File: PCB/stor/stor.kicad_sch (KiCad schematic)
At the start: 1 part, among them U1 STM32H723VGT6

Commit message: all sketched except power section
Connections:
- net GND: now reaches U1.10 (VSS)
- net GND: now also U1.19 (VSSA)
- net PH0: now reaches U1.12 (PH0-OSC_IN)
- net PH1: now reaches U1.13 (PH1-OSC_OUT)
- net VREF: now reaches U1.20 (VREF+)
- net VCAP1: now reaches U1.48 (VCAP)
- net SWDIO: now reaches U1.72 (PA13)
- net VCAP2: now reaches U1.73 (VCAP)
- net SWCLK: now reaches U1.76 (PA14)
- net PC14: now reaches U1.8 (PC14-OSC32_IN)
- net PC15: now reaches U1.9 (PC15-OSC32_OUT)
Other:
- note added: "2.2uf to gnd each"
- note added: "??"
- note added: "Crystal"
- note added: "swd debugging breakout"

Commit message: gnda, vss
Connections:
- net GND: now also U1.26 (VSS), U1.49 (VSS), U1.74 (VSS), U1.99 (VSS); no longer U1.19 (VSSA)
- new net GNDA: U1.19 (VSSA)

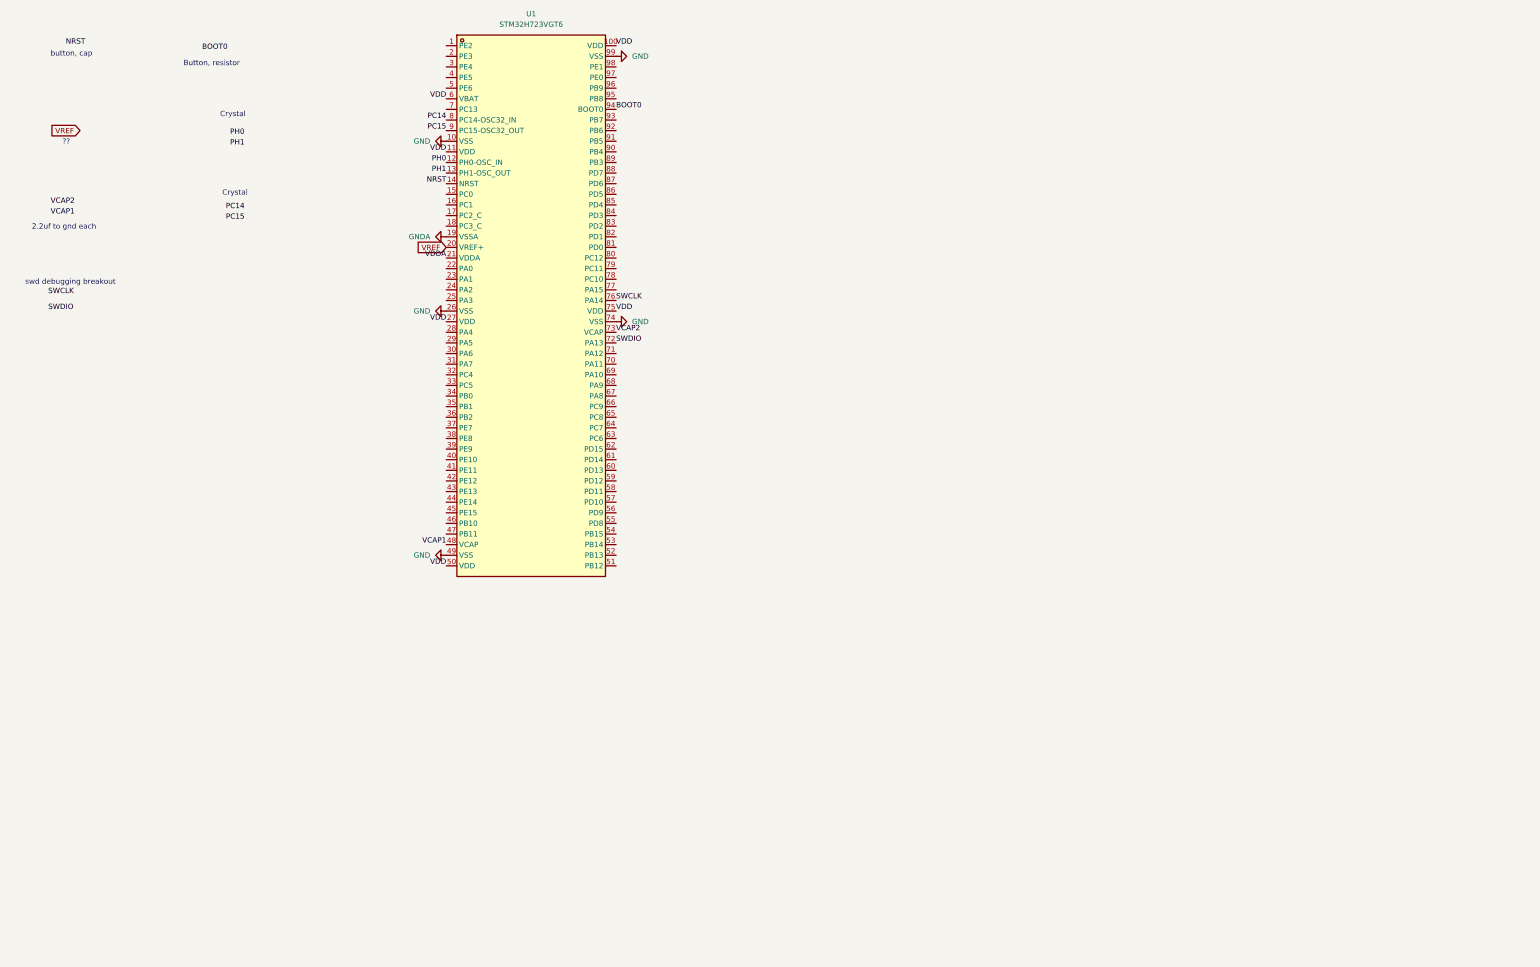
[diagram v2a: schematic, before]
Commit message: buck sourced
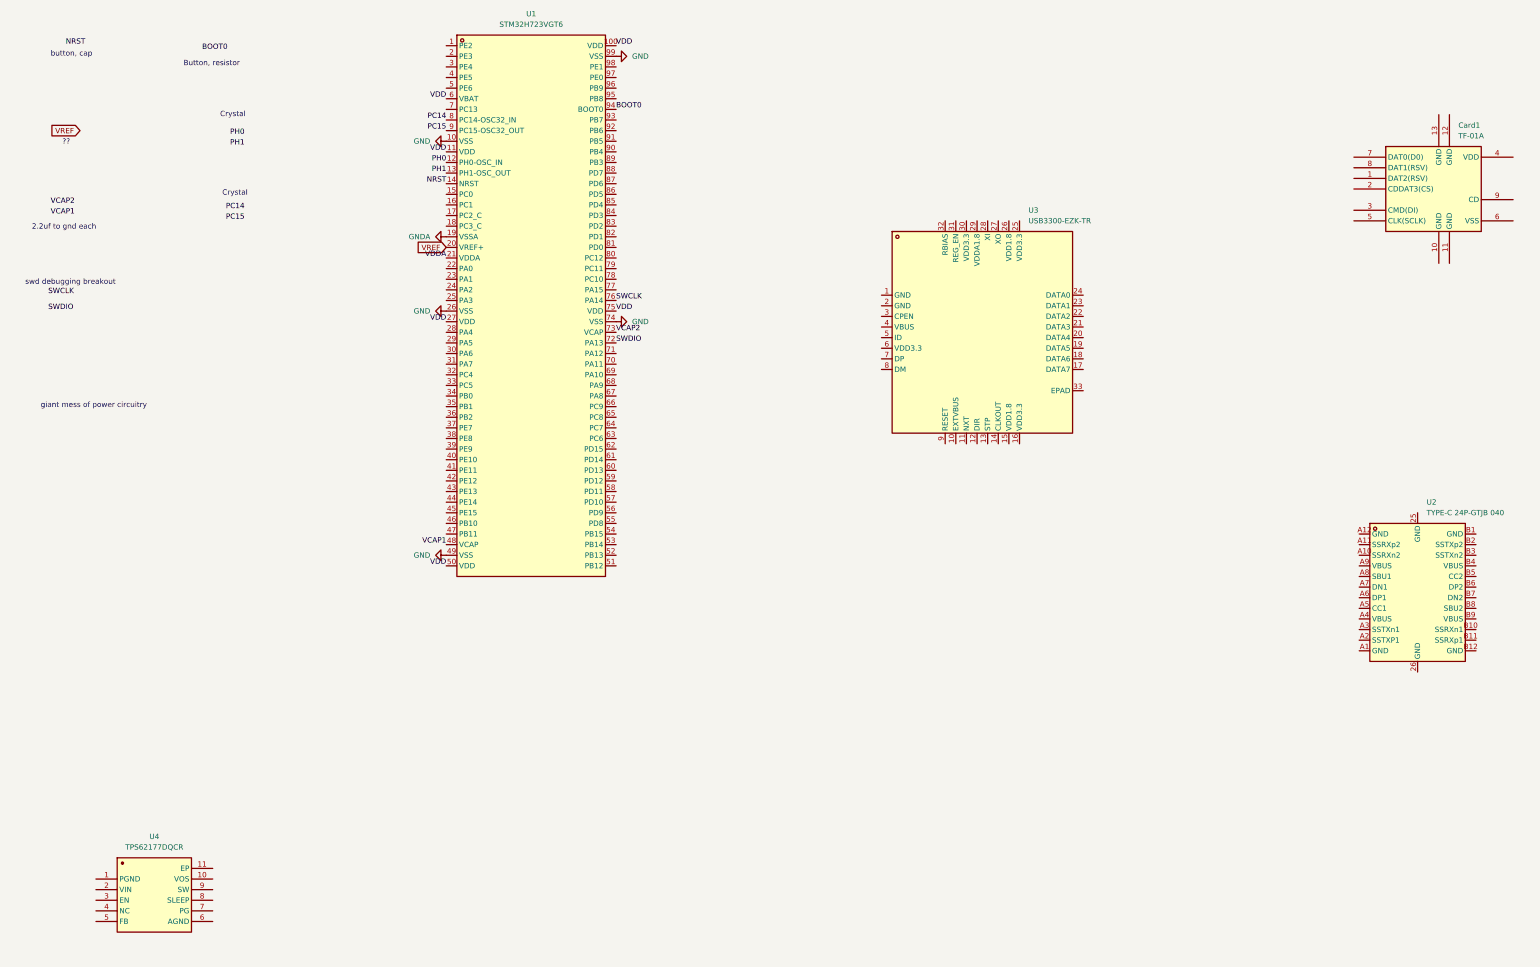
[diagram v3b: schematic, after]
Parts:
- added Card1: TF-01A, easyeda2kicad:TF-SMD_TF-01A, symbol easyeda2kicad:TF-01A
- added U2: TYPE-C 24P-GTJB 040, easyeda2kicad:USB-C-SMD_TYPE-C-24P-GTJB-040, symbol easyeda2kicad:TYPE-C24P-GTJB040
- added U3: USB3300-EZK-TR, easyeda2kicad:QFN-32_L5.0-W5.0-P0.50-BL-EP3.4, symbol easyeda2kicad:USB3300-EZK-TR
- added U4: TPS62177DQCR, easyeda2kicad:WSON-10_L3.0-W2.0-P0.50-BL-EP, symbol easyeda2kicad:TPS62177DQCR
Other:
- note added: "giant mess of power circuitry"

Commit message: smal
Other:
- note added: "8 100nF caps"
- note added: "Power"
- note removed: "giant mess of power circuitry"
- moved on the sheet: U2, U4
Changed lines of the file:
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@@
 	(generator_version "10.0")
 	(paper "A3")
-	(text "giant mess of power circuitry"
-		(exclude_from_sim no)
-		(at 32.512 108.966 0)
+	(rectangle
+		(start 30.48 180.34)
+		(end 153.67 241.3)
+		(stroke
+			(width 0)
+			(type default)
+		)
+		(fill
+			(type none)
+		)
+	)
+	(text "8 100nF caps"
+		(exclude_from_sim no)
+		(at 58.928 203.2 0)
 		(effects
 			(font
@@
 			(font
 				(size 1.27 1.27)
+			)
+		)
+	)
+	(text "Power"
+		(exclude_from_sim no)
+		(at 39.878 184.404 0)
+		(effects
+			(font
+				(size 2.54 2.54)
 			)
 		)
@@
 	(symbol
 		(lib_id "easyeda2kicad:TPS62177DQCR")
-		(at 46.99 226.06 0)
+		(at 118.11 212.09 0)
 		(unit 1)
 		(body_style 1)
@@
 		(fields_autoplaced yes)
 		(property "Reference" "U4"
-			(at 46.99 212.09 0)
+			(at 118.11 198.12 0)
 			(show_name no)
 			(do_not_autoplace no)
@@
 		)
 		(property "Value" "TPS62177DQCR"
-			(at 46.99 214.63 0)
+			(at 118.11 200.66 0)
 			(show_name no)
 			(do_not_autoplace no)
@@
 		)
 		(property "Footprint" "easyeda2kicad:WSON-10_L3.0-W2.0-P0.50-BL-EP"
-			(at 46.99 240.03 0)
+			(at 118.11 226.06 0)
 			(hide yes)
 			(show_name no)
@@
 		)
 		(property "Datasheet" "https://lcsc.com/product-detail/DC-DC-Converters_TI_TPS62177DQCR_TPS62177DQCR_C91241.html"
-			(at 46.99 242.57 0)
+			(at 118.11 228.6 0)
 			(hide yes)
 			(show_name no)
@@
 		)
 		(property "Description" ""
-			(at 46.99 226.06 0)
+			(at 118.11 212.09 0)
 			(hide yes)
 			(show_name no)
@@
 		)
 		(property "Manufacturer" "TI(德州仪器)"
-			(at 46.99 245.11 0)
+			(at 118.11 231.14 0)
 			(hide yes)
 			(show_name no)
@@
 		)
 		(property "MPN" "TPS62177DQCR"
-			(at 46.99 247.65 0)
+			(at 118.11 233.68 0)
 			(hide yes)
 			(show_name no)
@@
 		)
 		(property "LCSC Part" "C91241"
-			(at 46.99 250.19 0)
+			(at 118.11 236.22 0)
 			(hide yes)
 			(show_name no)
@@
 	(symbol
 		(lib_id "easyeda2kicad:TYPE-C24P-GTJB040")
-		(at 349.25 153.67 0)
+		(at 260.35 165.1 0)
 		(unit 1)
 		(body_style 1)
@@
 		(fields_autoplaced yes)
 		(property "Reference" "U2"
-			(at 351.3933 132.08 0)
+			(at 262.4933 143.51 0)
 			(show_name no)
 			(do_not_autoplace no)
@@
 		)
 		(property "Value" "TYPE-C 24P-GTJB 040"
-			(at 351.3933 134.62 0)
+			(at 262.4933 146.05 0)
 			(show_name no)
 			(do_not_autoplace no)
@@
 		)
 		(property "Footprint" "easyeda2kicad:USB-C-SMD_TYPE-C-24P-GTJB-040"
-			(at 349.25 180.34 0)
+			(at 260.35 191.77 0)
 			(hide yes)
 			(show_name no)
@@
 		)
 		(property "Datasheet" "https://www.lcsc.com/datasheet/C3151751.pdf"
-			(at 349.25 182.88 0)
+			(at 260.35 194.31 0)
 			(hide yes)
 			(show_name no)
@@
 		)
 		(property "Description" ""
-			(at 349.25 153.67 0)
+			(at 260.35 165.1 0)
 			(hide yes)
 			(show_name no)
@@
 		)
 		(property "Manufacturer" "SHOU HAN(首韩)"
-			(at 349.25 185.42 0)
+			(at 260.35 196.85 0)
 			(hide yes)
 			(show_name no)
@@
 		)
 		(property "MPN" "TYPE-C 24P-GTJB 040"
-			(at 349.25 187.96 0)
+			(at 260.35 199.39 0)
 			(hide yes)
 			(show_name no)
@@
 		)
 		(property "LCSC Part" "C3151751"
-			(at 349.25 190.5 0)
-			(hide yes)
-			(show_name no)
+			(at 260.35 201.93 0)
+			(hide yes)
+			(show_name no)

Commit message: stm and friends complete
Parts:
- added C1, C2: 2.2uF, easyeda2kicad:C0402, symbol easyeda2kicad:CL05A225KO5NQNC
- added C10, C15, C3, C4, C5, C6, C7, C8, C9: 100nF, easyeda2kicad:C0402, symbol easyeda2kicad:CC0402KRX7R7BB104
- added C11, C12: 10pF, easyeda2kicad:C0402, symbol easyeda2kicad:CC0402JRNPO9BN100
- added C13, C14: 12pF, easyeda2kicad:C0402, symbol easyeda2kicad:CC0402JRNPO9BN120
- added J1: Conn_01x04_Socket, symbol Connector:Conn_01x04_Socket
- added R1: 10k, easyeda2kicad:R0402, symbol easyeda2kicad:RC0402FR-0710KL
- added SW1, SW2: TS1603-TZ38HBM, easyeda2kicad:SW-SMD_4P-L4.5-W4.5-P3.00-LS6.8, symbol easyeda2kicad:TS1603-TZ38HBM
- added X1: 25mhz, easyeda2kicad:CRYSTAL-SMD_4P-L3.2-W2.5-BL, symbol easyeda2kicad:X322525MOB4SI
- added X2: 32.768k, easyeda2kicad:OSC-SMD_L3.2-W1.5, symbol easyeda2kicad:SC-32S32.768kHz20PPM12.5pF
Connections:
- net GNDA is gone; now on net GND: U1.19 (VSSA)
- net VDDA is gone; now on net VDD: U1.21 (VDDA)
- net BOOT0: now also R1.2, SW2.1 (A), SW2.2 (B)
- net GND: now also C1.1, C10.1, C11.1, C12.1, C13.1, C14.1, C15.1, C2.1, C3.1, C4.1, C5.1, C6.1, C7.1, C8.1, C9.1, J1.1 (Pin_1), R1.1, SW1.3 (C), SW1.4 (D), X1.2 (GND), X1.4 (GND)
- net NRST: now also C15.2, SW1.1 (A), SW1.2 (B)
- net PC14: now also C13.2, X2.2
- net PC15: now also C14.2, X2.1
- net PH0: now also C12.2, X1.3 (OSC2)
- net PH1: now also C11.2, X1.1 (OSC1)
- net SWCLK: now also J1.2 (Pin_2)
- net SWDIO: now also J1.3 (Pin_3)
- net VCAP1: now also C2.2
- net VCAP2: now also C1.2
- net VDD: now also C10.2, C3.2, C4.2, C5.2, C6.2, C7.2, C8.2, C9.2, J1.4 (Pin_4), SW2.3 (C), SW2.4 (D)
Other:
- note added: "STM and friends"
- note removed: "2.2uf to gnd each"
- note removed: "8 100nF caps"
- note removed: "Button, resistor"
- note removed: "Crystal"
- note removed: "swd debugging breakout"
- moved on the sheet: U4

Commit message: pmic done
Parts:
- added C16: 2.2uF, easyeda2kicad:C0402, symbol easyeda2kicad:CL05A225KO5NQNC
- added C17: 22uF, easyeda2kicad:C0402, symbol easyeda2kicad:GRM158C80G226ME01D
- added L1: 10uH, easyeda2kicad:IND-SMD_L3.2-W2.5_CKST322512-2.2UH, symbol easyeda2kicad:XRTC322512S100MBCA
- added R2, R3: 5.1k, easyeda2kicad:R0402, symbol easyeda2kicad:RC0402FR-075K1L
- added R4: 100k, easyeda2kicad:R0402, symbol easyeda2kicad:RC0402FR-07100KL
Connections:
- net GND: now also U2.25 (GND), U2.A1 (GND), U2.A12 (GND), U2.B1 (GND), U2.B12 (GND), U4.1 (PGND), U4.11 (EP), U4.4 (NC), U4.5 (FB), U4.6 (AGND), C16.2, C17.1, R2.1, R3.1
- net VDD: now also U4.10 (VOS), C17.2, L1.2, R4.2
- net VBUS: now reaches U4.2 (VIN)
- net VBUS: now also U2.A4 (VBUS), U2.A9 (VBUS), U2.B4 (VBUS), U2.B9 (VBUS), U4.3 (EN), C16.1
- net at U4.7 (PG): now also R4.1
- net at U4.9 (SW): now also L1.1
- net CC1: now reaches U2.A5 (CC1)
- net CC1: now also R2.2
- net D+: now reaches U2.A6 (DP1)
- net D+: now also U2.B6 (DP2)
- net D-: now reaches U2.A7 (DN1)
- net D-: now also U2.B7 (DN2)
- net CC2: now reaches U2.B5 (CC2)
- net CC2: now also R3.2
- no-connect marks 0 -> 11
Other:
- note added: "USBC"
- moved on the sheet: U2, U4
